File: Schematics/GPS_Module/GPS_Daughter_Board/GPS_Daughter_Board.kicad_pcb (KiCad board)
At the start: 2 copper layers, 50 x 65 mm, 17 parts, among them J2 470804001, U1 SAM-M10Q, U2 LM66100DCKR

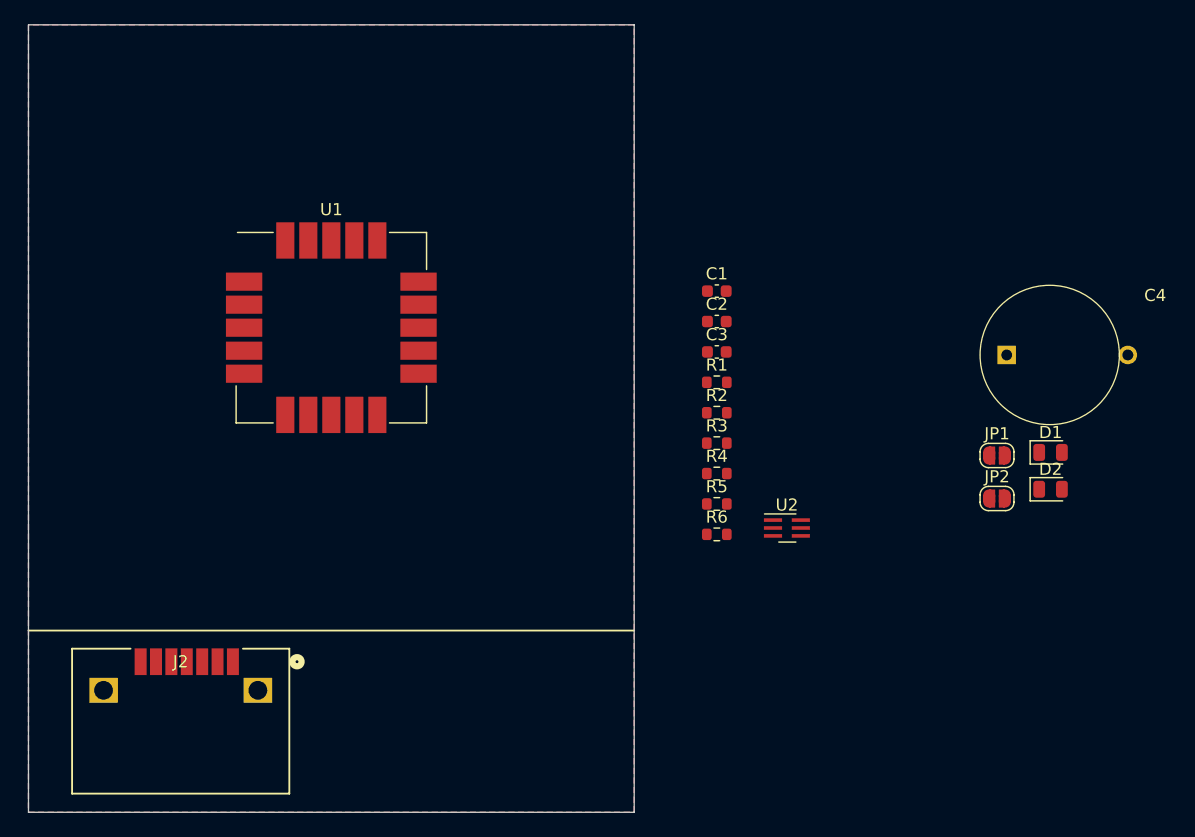
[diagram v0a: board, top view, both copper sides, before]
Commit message: finished daughter board waiting for approval
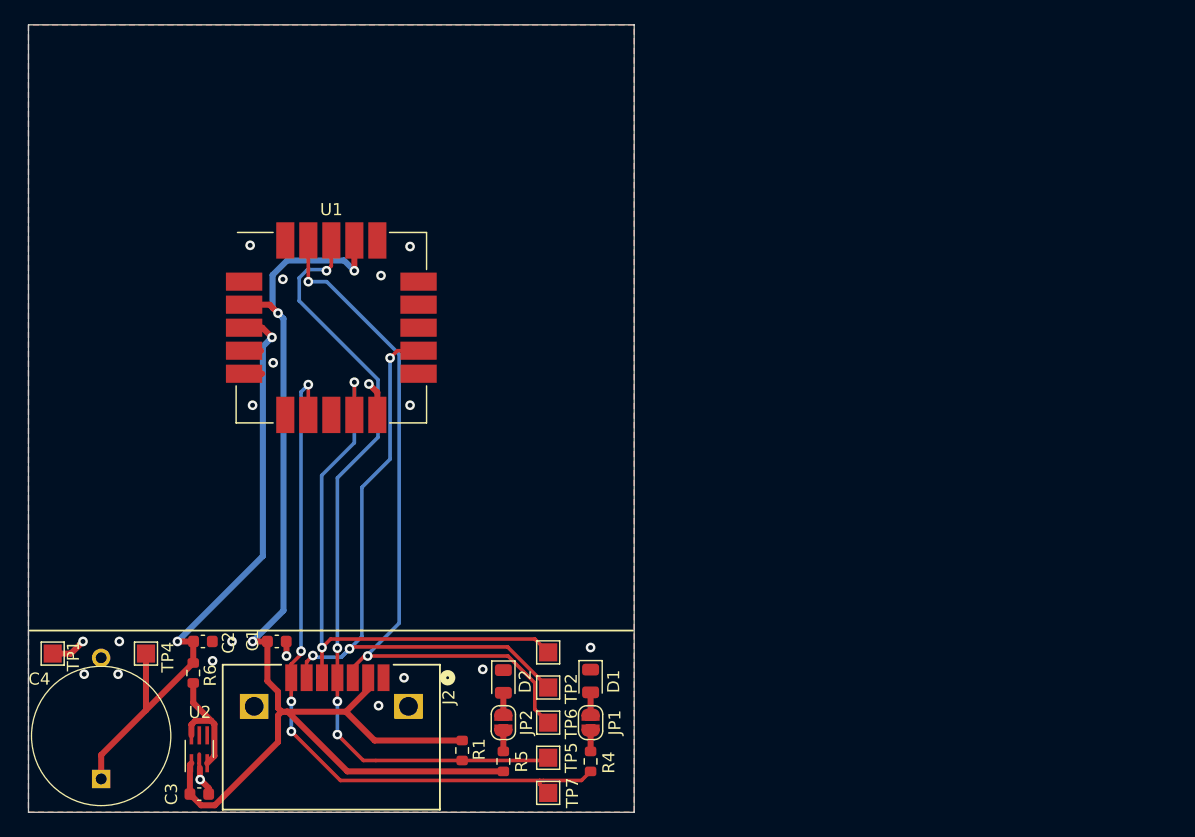
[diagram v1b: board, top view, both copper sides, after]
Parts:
- removed R2, R3: 2.2k, Resistor_SMD:R_0603_1608Metric
- added TP1: TP_PA0, TestPoint:TestPoint_Pad_1.5x1.5mm, F.Cu at (124.7, 126.1)
- added TP2: TP_PA0, TestPoint:TestPoint_Pad_1.5x1.5mm, F.Cu at (165.6, 128.9)
- added TP3: TP_PA0, TestPoint:TestPoint_Pad_1.5x1.5mm, F.Cu at (165.6, 126.0)
- added TP4: TP_PA0, TestPoint:TestPoint_Pad_1.5x1.5mm, F.Cu at (132.4, 126.1)
- added TP5: TP_PA0, TestPoint:TestPoint_Pad_1.5x1.5mm, F.Cu at (165.6, 134.7)
- added TP6: TP_PA0, TestPoint:TestPoint_Pad_1.5x1.5mm, F.Cu at (165.6, 131.8)
- added TP7: TP_PA0, TestPoint:TestPoint_Pad_1.5x1.5mm, F.Cu at (165.6, 137.6)
- moved C4 84.4 mm to (128.7, 132.9), turned to 90 degrees
- moved C3 56.2 mm to (136.8, 137.7)
- moved U2 51.8 mm to (136.8, 134.0), turned to 90 degrees
- moved C2 50.0 mm to (137.1, 125.1), turned to 180 degrees
- moved D2 47.9 mm to (161.9, 128.4), turned to -90 degrees
- moved C1 46.4 mm to (143.2, 125.1), turned to 180 degrees
- moved JP2 44.8 mm to (161.9, 131.8), turned to -90 degrees
- moved R6 44.7 mm to (136.3, 127.7), turned to 90 degrees
- moved D1 42.4 mm to (169.1, 128.4), turned to -90 degrees
- moved JP1 40.1 mm to (169.1, 131.8), turned to -90 degrees
- moved R1 37.0 mm to (158.5, 134.1), turned to -90 degrees
- moved R5 27.6 mm to (161.9, 135.0), turned to 90 degrees
- moved R4 25.9 mm to (169.1, 135.0), turned to 90 degrees
- moved J2 12.5 mm to (147.7, 133.0)
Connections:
- R1 pad 1: 3.3V -> GPS_3.3V
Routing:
- net GPS_3.3V: track 0.00 -> 106.8 mm, vias 0 -> 3
- net RST_GPS_D: track 0.00 -> 65.4 mm, vias 0 -> 4
- net EXTINT_GPS_D: track 0.00 -> 60.3 mm, vias 0 -> 2
- net PPS_GPS_D: track 0.00 -> 59.8 mm, vias 0 -> 4
- net SCL_GPS_D: track 0.00 -> 52.2 mm, vias 0 -> 3
- net GPS_BCKP_BATT: track 0.00 -> 51.7 mm, vias 0 -> 2
- net SDA_GPS_D: track 0.00 -> 47.9 mm, vias 0 -> 2
- net GPS_GND: track 0.00 -> 13.4 mm, vias 0 -> 20
- net Net-(U2-*CE): track 0.00 -> 10.3 mm
- net Net-(D1-A): track 0.00 -> 1.85 mm
- net Net-(D2-A): track 0.00 -> 1.81 mm
- net Net-(JP2-B): track 0.00 -> 1.73 mm
- net Net-(JP1-B): track 0.00 -> 1.73 mm

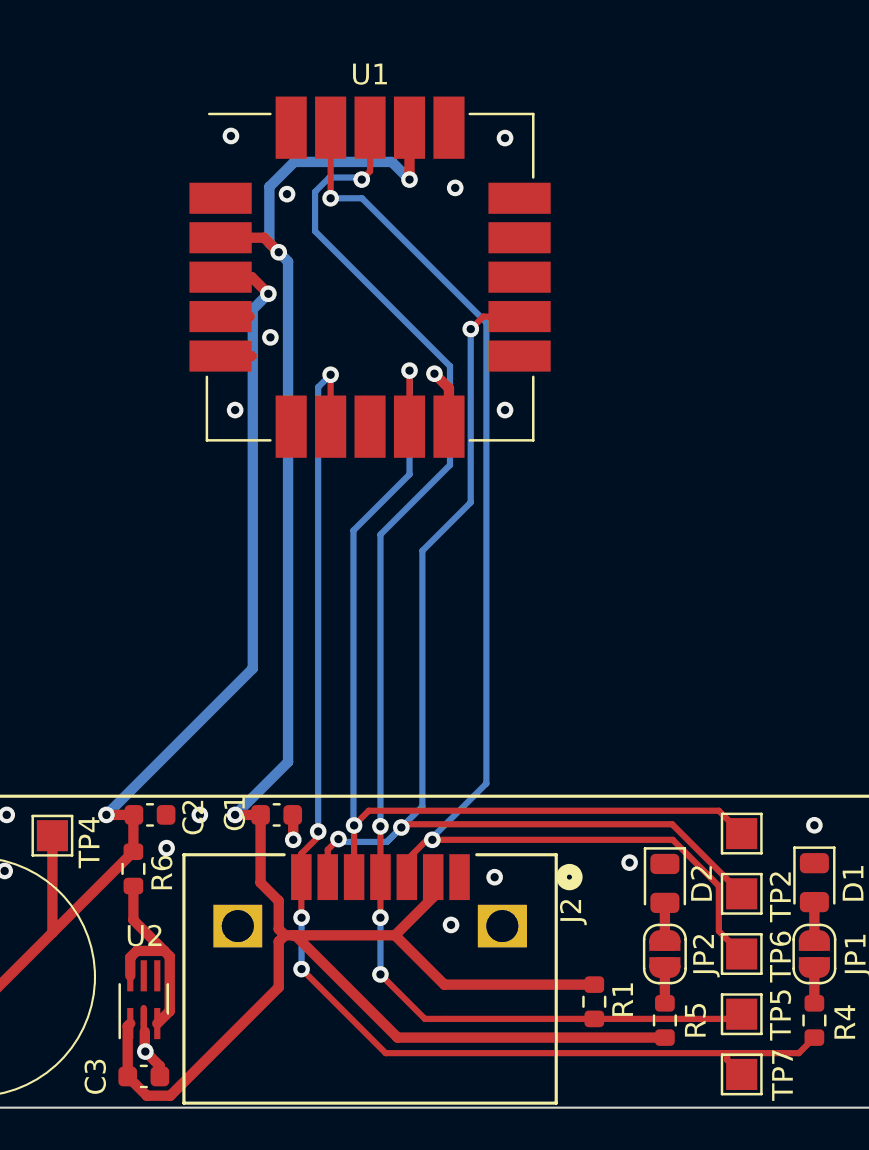
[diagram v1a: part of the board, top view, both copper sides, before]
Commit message: finished silkscreen for GPS module
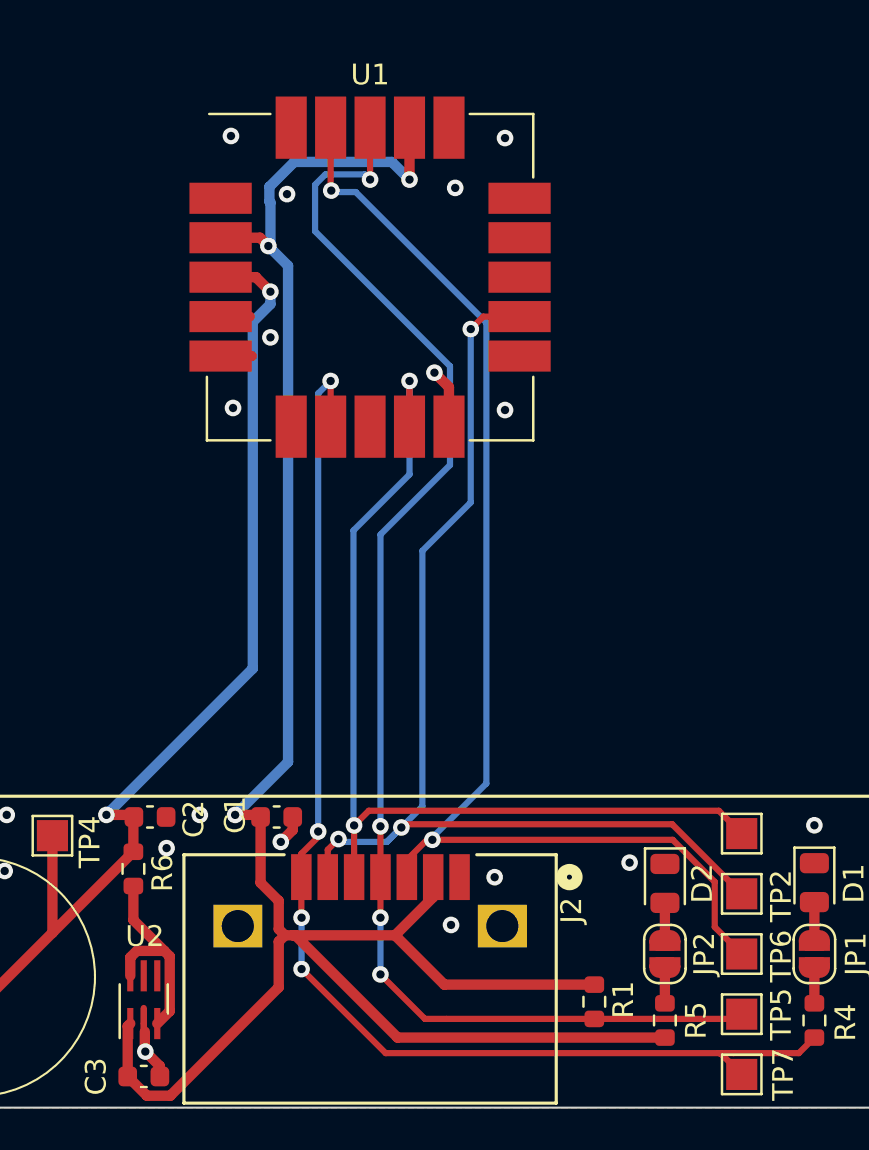
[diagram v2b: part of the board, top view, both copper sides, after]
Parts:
- moved C1 0.10 mm to (143.2, 125.2)
- moved C2 0.10 mm to (137.1, 125.2)
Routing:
- net SDA_GPS_D: track 47.9 -> 46.9 mm
- net RST_GPS_D: track 65.4 -> 66.0 mm
- net GPS_3.3V: track 106.8 -> 106.3 mm

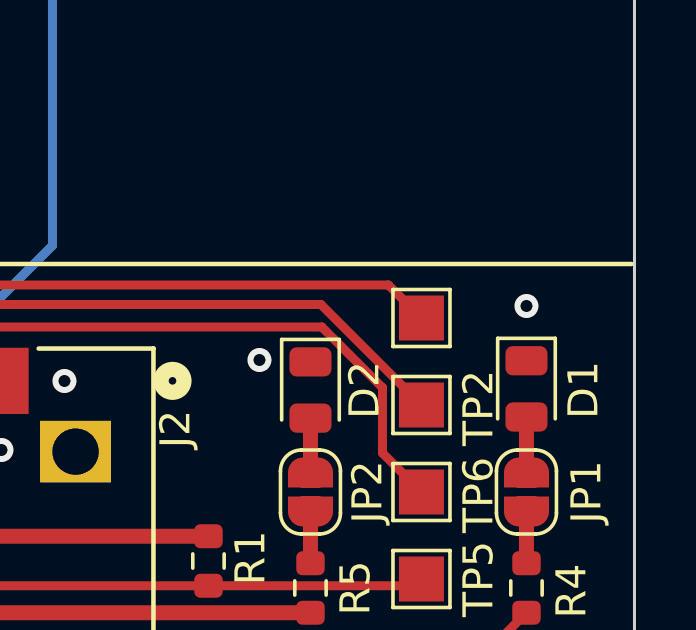
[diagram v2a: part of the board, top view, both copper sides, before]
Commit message: gps daughter board GND stiching
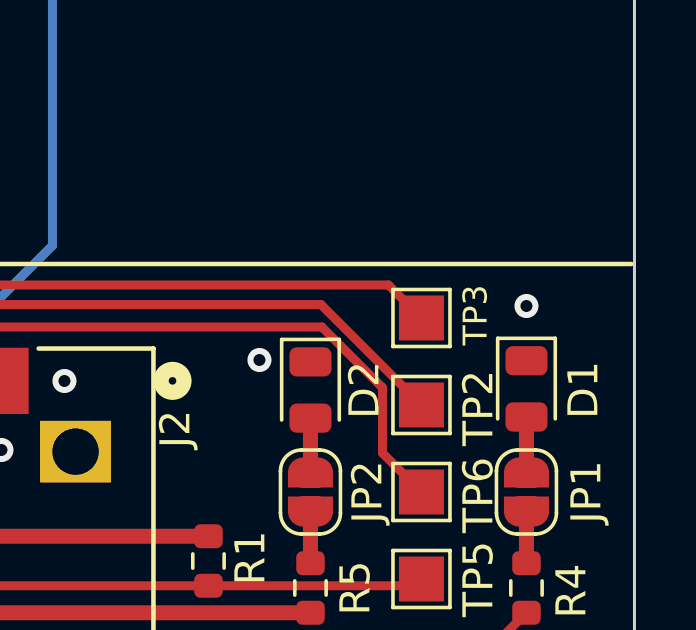
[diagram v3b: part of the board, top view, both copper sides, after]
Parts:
- turned TP3 to 0 degrees
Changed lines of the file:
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@@
     )
+  )
+  (footprint "TestPoint:TestPoint_Pad_1.5x1.5mm" (layer "F.Cu")
+    (at 165.6 126)
+    (descr "SMD rectangular pad as test Point, square 1.5mm side length")
+    (tags "test point SMD pad rectangle square")
+    (property "Sheetfile" "GPS_Daughter_Board.kicad_sch")
+    (property "Sheetname" "")
+    (property "ki_description" "test point")
+    (property "ki_keywords" "test point tp")
+    (attr exclude_from_pos_files)
+    (fp_text reference "TP3" (at 1.8 -0.1 90) (layer "F.SilkS")
+        (effects (font (size 0.8 0.8) (thickness 0.1)))
+    )
+    (fp_text value "TP_PA0" (at 0 1.75) (layer "F.Fab")
+        (effects (font (size 1 1) (thickness 0.15)))
+    )
+    (fp_text user "${REFERENCE}" (at 0 -1.65) (layer "F.Fab")
+        (effects (font (size 1 1) (thickness 0.15)))
+    )
+    (fp_line (start -0.95 -0.95) (end 0.95 -0.95)
+      (stroke (width 0.12) (type solid)) (layer "F.SilkS"))
+    (fp_line (start -0.95 0.95) (end -0.95 -0.95)
+      (stroke (width 0.12) (type solid)) (layer "F.SilkS"))
+    (fp_line (start 0.95 -0.95) (end 0.95 0.95)
+      (stroke (width 0.12) (type solid)) (layer "F.SilkS"))
+    (fp_line (start 0.95 0.95) (end -0.95 0.95)
+      (stroke (width 0.12) (type solid)) (layer "F.SilkS"))
+    (fp_line (start -1.25 -1.25) (end -1.25 1.25)
+      (stroke (width 0.05) (type solid)) (layer "F.CrtYd"))
+    (fp_line (start -1.25 -1.25) (end 1.25 -1.25)
+      (stroke (width 0.05) (type solid)) (layer "F.CrtYd"))
+    (fp_line (start 1.25 1.25) (end -1.25 1.25)
+      (stroke (width 0.05) (type solid)) (layer "F.CrtYd"))
+    (fp_line (start 1.25 1.25) (end 1.25 -1.25)
+      (stroke (width 0.05) (type solid)) (layer "F.CrtYd"))
+    (pad "1" smd rect (at 0 0) (size 1.5 1.5) (layers "F.Cu" "F.Mask")
+      (net 8 "SDA_GPS_D") (pinfunction "1") (pintype "passive"))
   )
   (footprint "RF_GPS:ublox_SAM-M8Q_HandSolder" (layer "F.Cu")
@@
     )
   )
-  (footprint "TestPoint:TestPoint_Pad_1.5x1.5mm" (layer "F.Cu")
-    (at 165.6 126 180)
-    (descr "SMD rectangular pad as test Point, square 1.5mm side length")
-    (tags "test point SMD pad rectangle square")
-    (property "Sheetfile" "GPS_Daughter_Board.kicad_sch")
-    (property "Sheetname" "")
-    (property "ki_description" "test point")
-    (property "ki_keywords" "test point tp")
-    (attr exclude_from_pos_files)
-    (fp_text reference "TP3" (at 0.1 -4.8) (layer "F.SilkS") hide
-        (effects (font (size 1 1) (thickness 0.15)))
-    )
-    (fp_text value "TP_PA0" (at 0 1.75) (layer "F.Fab")
-        (effects (font (size 1 1) (thickness 0.15)))
-    )
-    (fp_text user "${REFERENCE}" (at 0 -1.65) (layer "F.Fab")
-        (effects (font (size 1 1) (thickness 0.15)))
-    )
-    (fp_line (start -0.95 -0.95) (end 0.95 -0.95)
-      (stroke (width 0.12) (type solid)) (layer "F.SilkS"))
-    (fp_line (start -0.95 0.95) (end -0.95 -0.95)
-      (stroke (width 0.12) (type solid)) (layer "F.SilkS"))
-    (fp_line (start 0.95 -0.95) (end 0.95 0.95)
-      (stroke (width 0.12) (type solid)) (layer "F.SilkS"))
-    (fp_line (start 0.95 0.95) (end -0.95 0.95)
-      (stroke (width 0.12) (type solid)) (layer "F.SilkS"))
-    (fp_line (start -1.25 -1.25) (end -1.25 1.25)
-      (stroke (width 0.05) (type solid)) (layer "F.CrtYd"))
-    (fp_line (start -1.25 -1.25) (end 1.25 -1.25)
-      (stroke (width 0.05) (type solid)) (layer "F.CrtYd"))
-    (fp_line (start 1.25 1.25) (end -1.25 1.25)
-      (stroke (width 0.05) (type solid)) (layer "F.CrtYd"))
-    (fp_line (start 1.25 1.25) (end 1.25 -1.25)
-      (stroke (width 0.05) (type solid)) (layer "F.CrtYd"))
-    (pad "1" smd rect (at 0 0 180) (size 1.5 1.5) (layers "F.Cu" "F.Mask")
-      (net 8 "SDA_GPS_D") (pinfunction "1") (pintype "passive"))
-  )
   (footprint "Resistor_SMD:R_0603_1608Metric" (layer "F.Cu")
